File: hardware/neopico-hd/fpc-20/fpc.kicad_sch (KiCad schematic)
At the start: 2 parts, among them J1 Conn_02x27_Pin, J2 Conn_01x20_Pin

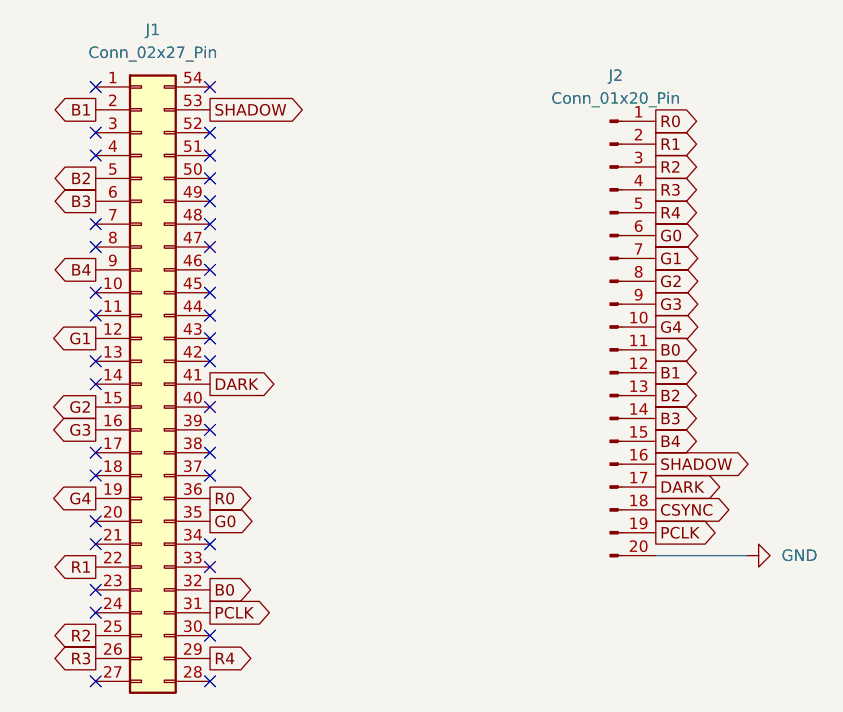
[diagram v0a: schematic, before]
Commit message: Add GND plane
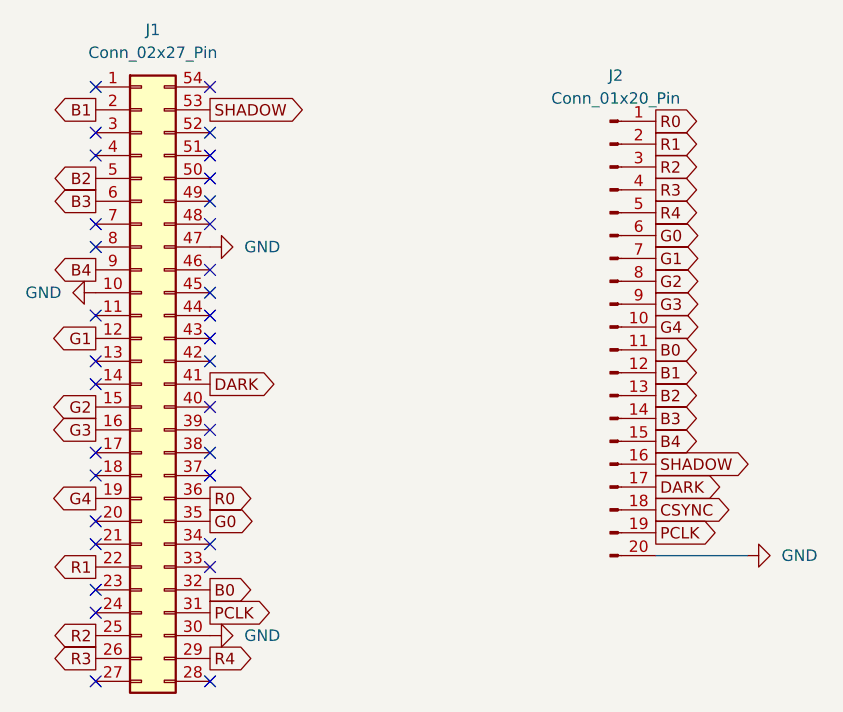
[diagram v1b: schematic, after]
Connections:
- net GND: now also J1.10 (Pin_10), J1.30 (Pin_30), J1.47 (Pin_47)
- no-connect marks 36 -> 33
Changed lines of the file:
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@@
-	)
-	(no_connect
-		(at 105.41 76.2)
 	)
 	(no_connect
@@
 	)
 	(no_connect
-		(at 92.71 81.28)
-	)
-	(no_connect
 		(at 105.41 73.66)
 	)
@@
 	(no_connect
 		(at 105.41 68.58)
-	)
-	(no_connect
-		(at 105.41 119.38)
 	)
 	(no_connect
@@
 				(justify left)
 				(hide yes)
+			)
+		)
+	)
+	(symbol
+		(lib_id "power:GND")
+		(at 92.71 81.28 270)
+		(unit 1)
+		(exclude_from_sim no)
+		(in_bom yes)
+		(on_board yes)
+		(dnp no)
+		(fields_autoplaced yes)
+		(property "Reference" "#PWR02"
+			(at 86.36 81.28 0)
+			(effects
+				(font
+					(size 1.27 1.27)
+				)
+				(hide yes)
+			)
+		)
+		(property "Value" "GND"
+			(at 88.9 81.2799 90)
+			(effects
+				(font
+					(size 1.27 1.27)
+				)
+				(justify right)
+			)
+		)
+		(property "Footprint" ""
+			(at 92.71 81.28 0)
+			(effects
+				(font
+					(size 1.27 1.27)
+				)
+				(hide yes)
+			)
+		)
+		(property "Datasheet" ""
+			(at 92.71 81.28 0)
+			(effects
+				(font
+					(size 1.27 1.27)
+				)
+				(hide yes)
+			)
+		)
+		(property "Description" "Power symbol creates a global label with name \"GND\" , ground"
+			(at 92.71 81.28 0)
+			(effects
+				(font
+					(size 1.27 1.27)
+				)
+				(hide yes)
+			)
+		)
+		(pin "1"
+		)
+		(instances
+			(project "fpc"
+				(path "/291ca268-9774-44b9-b178-17e1aebe9cc2"
+					(reference "#PWR02")
+					(unit 1)
+				)
+			)
+		)
+	)
+	(symbol
+		(lib_id "power:GND")
+		(at 105.41 76.2 90)
+		(unit 1)
+		(exclude_from_sim no)
+		(in_bom yes)
+		(on_board yes)
+		(dnp no)
+		(fields_autoplaced yes)
+		(property "Reference" "#PWR01"
+			(at 111.76 76.2 0)
+			(effects
+				(font
+					(size 1.27 1.27)
+				)
+				(hide yes)
+			)
+		)
+		(property "Value" "GND"
+			(at 109.22 76.1999 90)
+			(effects
+				(font
+					(size 1.27 1.27)
+				)
+				(justify right)
+			)
+		)
+		(property "Footprint" ""
+			(at 105.41 76.2 0)
+			(effects
+				(font
+					(size 1.27 1.27)
+				)
+				(hide yes)
+			)
+		)
+		(property "Datasheet" ""
+			(at 105.41 76.2 0)
+			(effects
+				(font
+					(size 1.27 1.27)
+				)
+				(hide yes)
+			)
+		)
+		(property "Description" "Power symbol creates a global label with name \"GND\" , ground"
+			(at 105.41 76.2 0)
+			(effects
+				(font
+					(size 1.27 1.27)
+				)
+				(hide yes)
+			)
+		)
+		(pin "1"
+		)
+		(instances
+			(project ""
+				(path "/291ca268-9774-44b9-b178-17e1aebe9cc2"
+					(reference "#PWR01")
+					(unit 1)
+				)
 			)
 		)
@@
 					(unit 1)
 				)
+			)
+		)
+	)
+	(symbol
+		(lib_id "power:GND")
+		(at 105.41 119.38 90)
+		(unit 1)
+		(exclude_from_sim no)
+		(in_bom yes)
+		(on_board yes)
+		(dnp no)
+		(fields_autoplaced yes)
+		(property "Reference" "#PWR03"
+			(at 111.76 119.38 0)
+			(effects
+				(font
+					(size 1.27 1.27)
+				)
+				(hide yes)
+			)
+		)
+		(property "Value" "GND"
+			(at 109.22 119.3799 90)
+			(effects
+				(font
+					(size 1.27 1.27)
+				)
+				(justify right)
+			)
+		)
+		(property "Footprint" ""
+			(at 105.41 119.38 0)
+			(effects
+				(font
+					(size 1.27 1.27)
+				)
+				(hide yes)
+			)
+		)
+		(property "Datasheet" ""
+			(at 105.41 119.38 0)
+			(effects
+				(font
+					(size 1.27 1.27)
+				)
+				(hide yes)
+			)
+		)
+		(property "Description" "Power symbol creates a global label with name \"GND\" , ground"
+			(at 105.41 119.38 0)
+			(effects
+				(font
+					(size 1.27 1.27)
+				)
+				(hide yes)
+			)
+		)
+		(pin "1"
+		)
+		(instances
+			(project "fpc"
+				(path "/291ca268-9774-44b9-b178-17e1aebe9cc2"
+					(reference "#PWR03")
+					(unit 1)
+				)
